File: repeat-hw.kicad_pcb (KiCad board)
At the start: 2 copper layers, 141 parts, among them J1 USB_C_Receptacle_USB2.0, J2 ARJM11C7-114-BA-EW2, J3 Conn_Coaxial, T1 FA2805, U1 nRF5340-QKxx, U10 USBLC6-2SC6, U11 USBLC6-2SC6, U2 USBLC6-2SC6, U3 W5100S, U4 TLV431DBZ, U5 VO618A, U6 SI3402, U7 nRF21540, U8 VO618A, U9 AMS1117-3.3, Y1 32MHz, Y2 25MHz

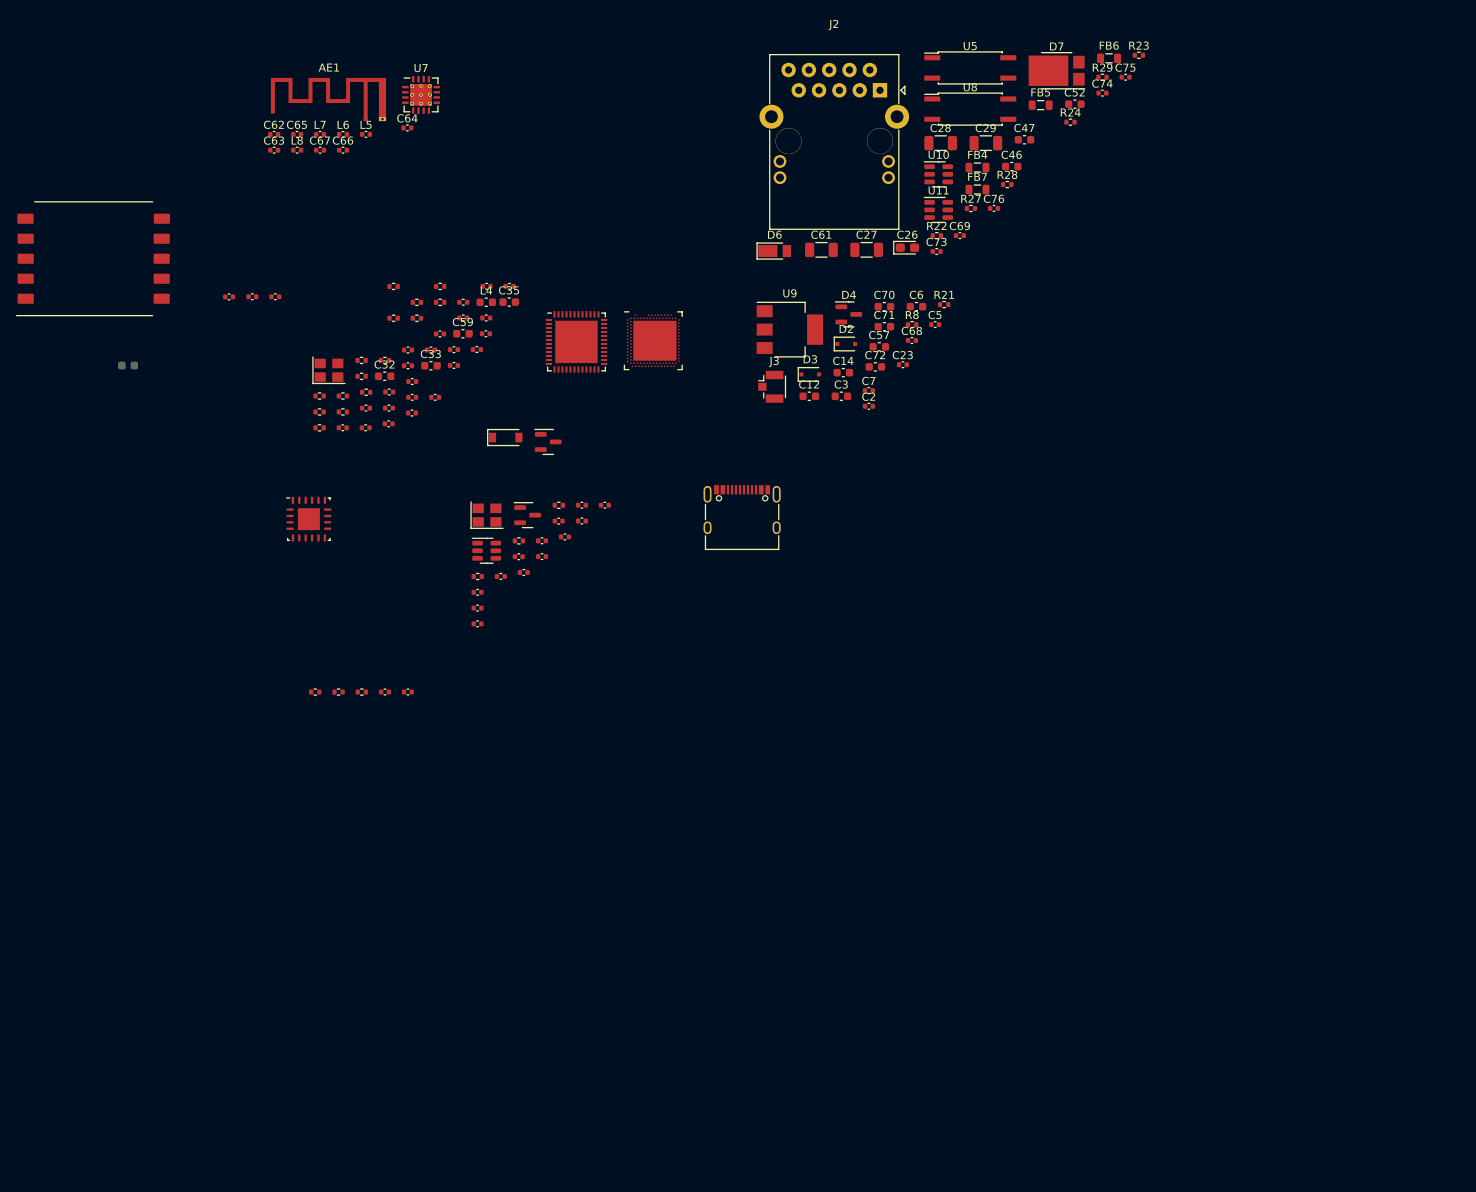
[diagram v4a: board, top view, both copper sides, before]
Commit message: Routing half done
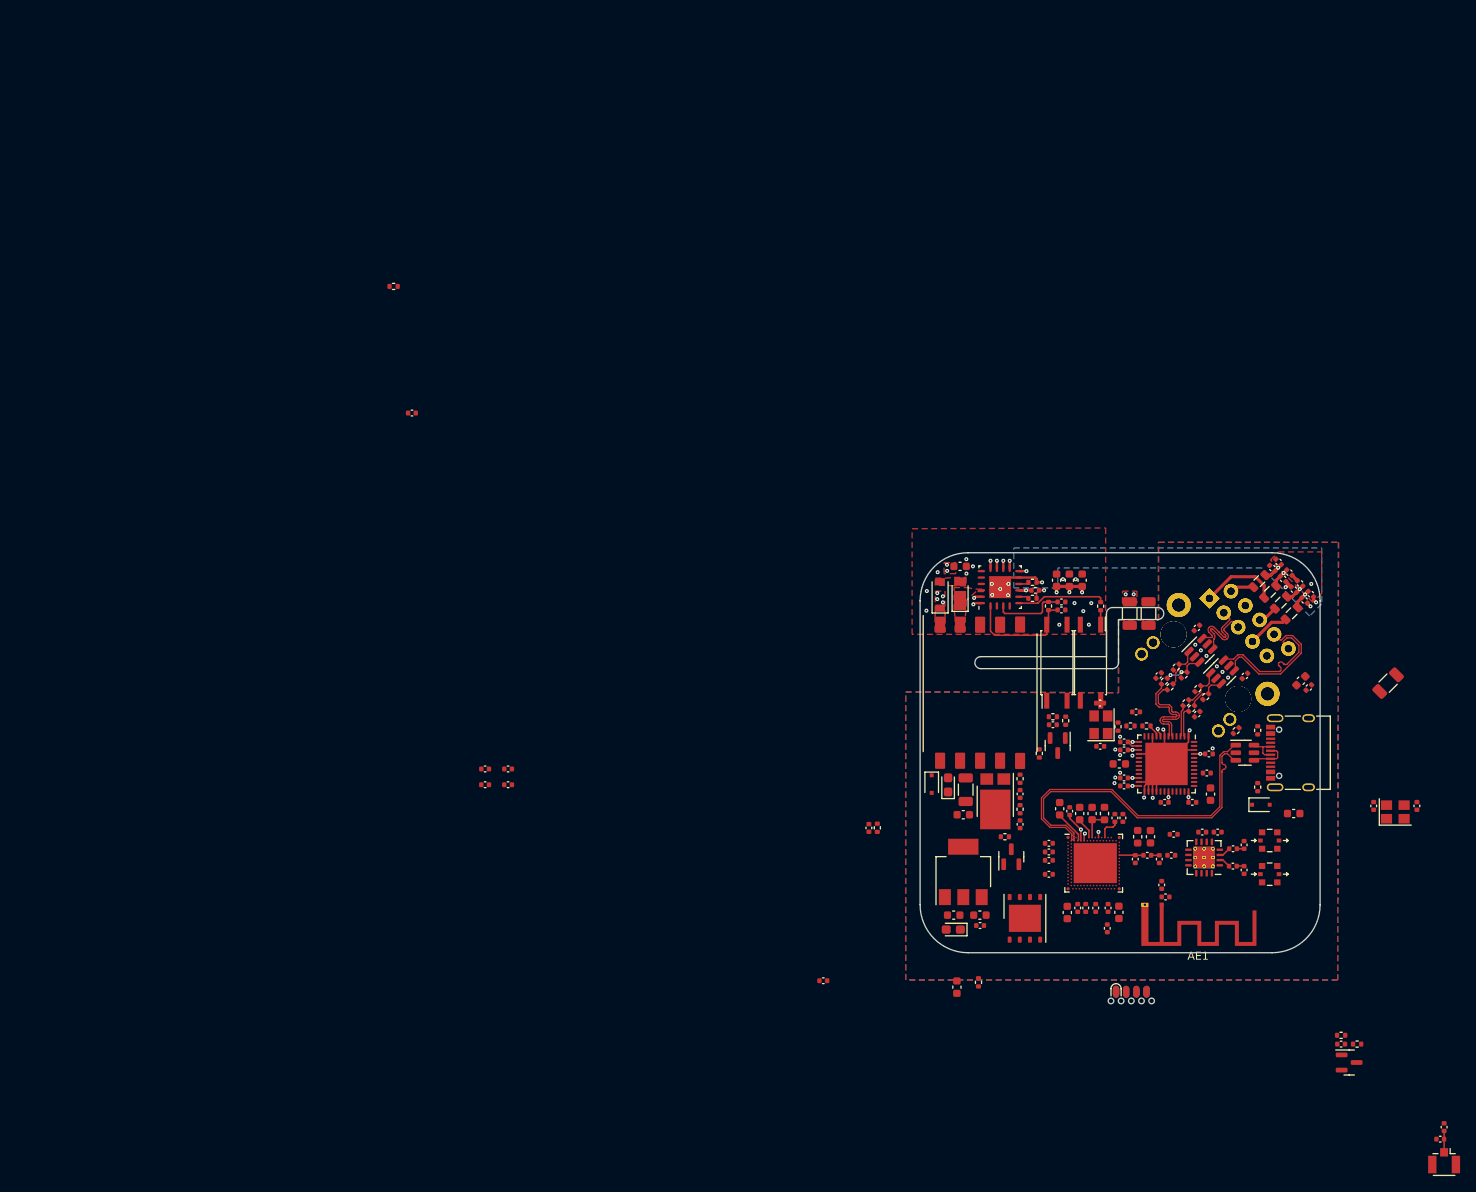
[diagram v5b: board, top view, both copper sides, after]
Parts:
- added C58: 47u, Capacitor_Tantalum_SMD:CP_EIA-2012-12_Kemet-R, F.Cu at (134.9, 126.7)
- added C77: TBD, Capacitor_SMD:C_0402_1005Metric, F.Cu at (79.3, 108.6)
- added C78: TBD, Capacitor_SMD:C_0402_1005Metric, F.Cu at (76.4, 108.6)
- added C79: TBD, Capacitor_SMD:C_0402_1005Metric, F.Cu at (79.3, 106.6)
- added C80: TBD, Capacitor_SMD:C_0402_1005Metric, F.Cu at (76.4, 106.6)
- added C81: 100n, Capacitor_SMD:C_0402_1005Metric, F.Cu at (118.7, 133.1)
- added C82: 100n, Capacitor_SMD:C_0402_1005Metric, F.Cu at (146.9, 118.0)
- added C83: 100n, Capacitor_SMD:C_0402_1005Metric, F.Cu at (156.2, 112.8)
- added C84: 100n, Capacitor_SMD:C_0402_1005Metric, F.Cu at (149.5, 111.9)
- added J2: ARJM11C7-114-BA-EW2, abracon:ARJM11C7-114-BA-EW2, B.Cu at (166.5, 93.8)
- added J4: Programming header, soicbite:SOIC_clipProgSmall, F.Cu at (157.2, 133.7)
- added L1: 10u, Inductor_SMD:L_0603_1608Metric, F.Cu at (158.0, 115.1)
- added L3: 10u, Inductor_SMD:L_0603_1608Metric, F.Cu at (153.8, 112.2)
- added TP1: MM8130-2600, murrata:MM8130-2600, F.Cu at (174.5, 115.6)
- added TP2: MM8130-2600, murrata:MM8130-2600, F.Cu at (174.5, 119.8)
- added U12: MX25R3235FZNxx0, Package_SON:WSON-8-1EP_6x5mm_P1.27mm_EP3.4x4mm, F.Cu at (143.9, 125.3)
- C1: moved to F.Cu
- C31: footprint Capacitor_SMD:C_0402_1005Metric -> Capacitor_SMD:C_0603_1608Metric
- C46, C47: value 3u3 -> 4u7
- J2: moved to B.Cu
- J3: value Conn_Coaxial -> ANT2
- moved C63 191.1 mm to (195.8, 152.9), turned to 180 degrees
- moved L6 185.3 mm to (196.3, 151.4), turned to 90 degrees
- moved C65 148.0 mm to (171.3, 116.1), turned to 90 degrees
- moved C62 146.6 mm to (161.5, 122.6)
- moved L7 146.2 mm to (169.9, 118.8), turned to 180 degrees
- moved L8 146.0 mm to (169.9, 116.6), turned to 180 degrees
- moved AE1 139.8 mm to (161.0, 123.6), turned to 180 degrees
- moved C64 139.8 mm to (171.3, 119.3), turned to -90 degrees
- moved C49 139.7 mm to (178.9, 85.6), turned to -45 degrees
- moved C67 139.4 mm to (166.1, 114.5), turned to 180 degrees
- moved C66 138.6 mm to (168.0, 114.5)
- moved L5 136.7 mm to (161.0, 121.1), turned to 90 degrees
- moved U7 136.6 mm to (166.3, 117.7), turned to 180 degrees
- moved R3 135.2 mm to (183.4, 139.9)
- moved R4 132.0 mm to (185.4, 141.0)
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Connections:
- net /~{SPIM_CS} renamed /~{ETH_CS}
- net Net-(J2-Pad3) renamed /W5100 + PoE/CON_RD-
- net Net-(J2-Pad5) renamed /W5100 + PoE/CON_RD+
- AE1 pad 1: GND -> Net-(C62-Pad1)
- AE1 pad 2: Net-(AE1-Pad2) -> GND
- C62 pad 1: Net-(AE1-Pad2) -> Net-(C62-Pad1)
- J2 pad 10: Net-(J2-Pad10) -> /W5100 + PoE/CON_TD+
- J2 pad 8: Net-(J2-Pad8) -> /W5100 + PoE/CON_TD-
- L5 pad 1: Net-(AE1-Pad2) -> Net-(C62-Pad1)
- L5 pad 2: Net-(C64-Pad1) -> Net-(L5-Pad2)
- L6 pad 2: Net-(C65-Pad1) -> Net-(L6-Pad2)
- U1 pad AK10: unconnected-(U1-PadAK10) -> /QSPI2
- U1 pad AK12: unconnected-(U1-PadAK12) -> /QSPI_CLK
- U1 pad AK14: unconnected-(U1-PadAK14) -> /~{QSPI_CS}
- U1 pad AK16: unconnected-(U1-PadAK16) -> /~{ETH_RST}
- U1 pad AK18: unconnected-(U1-PadAK18) -> /FEM_MODE
- U1 pad AK20: unconnected-(U1-PadAK20) -> /FEM_RXEN
- U1 pad AK28: unconnected-(U1-PadAK28) -> /FEM_ANTSEL
- U1 pad AK8: unconnected-(U1-PadAK8) -> /QSPI1
- U1 pad AL13: unconnected-(U1-PadAL13) -> /~{ETH_INT}
- U1 pad AL15: unconnected-(U1-PadAL15) -> /~{FEM_CS}
- U1 pad AL27: unconnected-(U1-PadAL27) -> /FEM_TXEN
- U1 pad AL29: unconnected-(U1-PadAL29) -> /~{FEM_PDN}
- U1 pad AL5: /~{INT} -> /QSPI0
- U1 pad AL9: unconnected-(U1-PadAL9) -> /QSPI3
- U1 pad V2: unconnected-(U1-PadV2) -> /USENSE_USB
- U1 pad Y2: unconnected-(U1-PadY2) -> /USENSE_POE
- U11 pad 1: /W5100 + PoE/TD- -> /W5100 + PoE/TD+
- U11 pad 3: /W5100 + PoE/TD+ -> /W5100 + PoE/TD-
- U11 pad 4: Net-(J2-Pad10) -> /W5100 + PoE/CON_TD-
- U11 pad 6: Net-(J2-Pad8) -> /W5100 + PoE/CON_TD+
- U3 pad 2: /W5100 + PoE/TD- -> /W5100 + PoE/ESD_TD-
- U3 pad 3: /W5100 + PoE/TD+ -> /W5100 + PoE/ESD_TD+
- U3 pad 47: /~{INT} -> /~{ETH_INT}
- U3 pad 48: /~{RESET} -> /~{ETH_RST}
- U3 pad 49: (no net) -> GND
- U3 pad 5: /W5100 + PoE/RD- -> /W5100 + PoE/ESD_RD-
- U3 pad 6: /W5100 + PoE/RD+ -> /W5100 + PoE/ESD_RD+
- U6 pad 21: (no net) -> Net-(C45-Pad2)
- U7 pad 11: unconnected-(U7-Pad11) -> /~{FEM_PDN}
- U7 pad 12: unconnected-(U7-Pad12) -> /SPIM_CLK
- U7 pad 13: unconnected-(U7-Pad13) -> /SPIM_MOSI
- U7 pad 14: unconnected-(U7-Pad14) -> /SPIM_MISO
- U7 pad 15: unconnected-(U7-Pad15) -> /~{FEM_CS}
- U7 pad 4: unconnected-(U7-Pad4) -> /FEM_MODE
- U7 pad 7: unconnected-(U7-Pad7) -> /FEM_RXEN
- U7 pad 8: unconnected-(U7-Pad8) -> /FEM_ANTSEL
- U7 pad 9: unconnected-(U7-Pad9) -> /FEM_TXEN
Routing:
- net Net-(C50-Pad2): track 0.00 -> 44.8 mm, vias 0 -> 2
- net Net-(C54-Pad2): track 0.00 -> 43.8 mm, vias 0 -> 2
- net Net-(C48-Pad2): track 0.00 -> 43.5 mm, vias 0 -> 2
- net /ESD_D-: track 0.00 -> 41.6 mm
- net /ESD_D+: track 0.00 -> 41.6 mm
- net GND: track 0.00 -> 40.5 mm, vias 0 -> 18
- net Net-(C44-Pad2): track 0.00 -> 35.2 mm, vias 0 -> 2
- net /W5100 + PoE/CON_TD+: track 0.00 -> 17.2 mm
- net /W5100 + PoE/CON_TD-: track 0.00 -> 17.1 mm
- net Net-(C34-Pad1): track 0.00 -> 14.7 mm
- net /W5100 + PoE/ESD_RD+: track 0.00 -> 11.6 mm
- net /W5100 + PoE/ESD_RD-: track 0.00 -> 11.4 mm
- net Net-(R28-Pad2): track 0.00 -> 11.1 mm
- net Net-(C28-Pad2): track 0.00 -> 11.0 mm, vias 0 -> 16
- net Net-(FB4-Pad2): track 0.00 -> 9.96 mm
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- added copper zone on B.Cu, net GND
- added copper zone on F.Cu, net GND
- added copper zone on In1.Cu, net GND
- added copper zone on In4.Cu, net GND
- added copper zone on F.Cu, net Net-(C28-Pad2)
- added copper zone on In2.Cu, net Net-(C28-Pad2)
- added copper zone on F.Cu, net Net-(C29-Pad2)
- added copper zone on F.Cu, net Net-(C32-Pad2)
- added copper zone on In1.Cu, net Net-(C32-Pad2)
- added copper zone on In4.Cu, net Net-(C32-Pad2)
- added copper zone on B.Cu, net Net-(C45-Pad2)
- added copper zone on F.Cu, net Net-(D5-Pad2)
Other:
- board outline added: 50 x 50 mm
- copper layers 2 -> 6

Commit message: More routing
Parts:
- moved C7 11.0 mm to (133.9, 116.2)
- moved C58 9.67 mm to (137.2, 117.3), turned to 0 degrees
- moved C70 9.56 mm to (137.2, 115.6), turned to 0 degrees
- moved C57 8.64 mm to (133.9, 117.5)
- moved D2 3.69 mm to (132.5, 112.2), turned to 90 degrees
- moved U9 3.26 mm to (136.0, 122.8), turned to -90 degrees
- moved C26 1.80 mm to (132.5, 108.6)
- moved L4 0.76 mm to (135.8, 113.0), turned to 90 degrees
- moved C27 0.70 mm to (135.8, 109.2)
- moved D7 0.64 mm to (139.6, 110.7)
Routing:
- net /W5100 + PoE/5V: track 0.00 -> 1.07 mm, vias 0 -> 3
- net GND: vias 18 -> 37
- net +3V3: vias 4 -> 15
- added copper zone on F.Cu, net +3V3
- added copper zone on F.Cu, net +5V
- added copper zone on F.Cu, net /W5100 + PoE/5V
- added copper zone on In2.Cu, net /W5100 + PoE/5V
- added copper zone on F.Cu, net Net-(C27-Pad1)
- added copper zone on F.Cu, net Net-(D7-Pad1)

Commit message: Routing almost done
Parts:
- AE1: footprint RF_Antenna:Texas_SWRA117D_2.4GHz_Left -> RF_Antenna:Texas_SWRA117D_2.4GHz_Right
- C26: value 470u -> 220u; footprint Capacitor_Tantalum_SMD:CP_EIA-2012-12_Kemet-R -> Capacitor_SMD:CP_Elec_5x5.3
- C58: value 47u -> 10u; footprint Capacitor_Tantalum_SMD:CP_EIA-2012-12_Kemet-R -> Capacitor_SMD:C_0603_1608Metric
- moved R25 107.4 mm to (162.1, 92.2)
- moved C56 98.8 mm to (159.0, 98.8), turned to 180 degrees
- moved C77 66.4 mm to (127.8, 154.0)
- moved C78 66.4 mm to (124.9, 154.0)
- moved C79 66.4 mm to (127.8, 152.0)
- moved C80 66.4 mm to (124.9, 152.0)
- moved J3 46.9 mm to (159.2, 127.0)
- moved L6 46.9 mm to (159.2, 122.8)
- moved C63 46.9 mm to (158.7, 124.2)
- moved C4 38.7 mm to (154.3, 108.2)
- moved C9 38.7 mm to (148.9, 108.2)
- moved Y1 38.7 mm to (151.6, 108.9)
- moved C10 35.2 mm to (159.2, 119.3), turned to 0 degrees
- moved R2 32.8 mm to (157.7, 119.8), turned to 90 degrees
- moved C23 30.9 mm to (178.3, 110.5)
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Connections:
- C29 pad 2: Net-(C29-Pad2) -> Earth
- C45 pad 2: Net-(C45-Pad2) -> Earth
- C49 pad 2: Net-(C45-Pad2) -> Earth
- C51 pad 2: Net-(C45-Pad2) -> Earth
- C55 pad 2: Net-(C45-Pad2) -> Earth
- D6 pad 1: Net-(C29-Pad2) -> Net-(D6-Pad1)
- L5 pad 2: Net-(L5-Pad2) -> Net-(TP2-PadA)
- L6 pad 2: Net-(L6-Pad2) -> Net-(TP1-PadA)
- R16 pad 2: Net-(C45-Pad2) -> Earth
- T1 pad 2: Net-(C29-Pad2) -> Net-(D6-Pad1)
- TP1 pad A: Net-(L5-Pad2) -> Net-(TP1-PadA)
- TP2 pad A: Net-(L6-Pad2) -> Net-(TP2-PadA)
- U6 pad 18: Net-(C29-Pad2) -> Net-(D6-Pad1)
- U6 pad 21: Net-(C45-Pad2) -> Earth
- U6 pad 9: Net-(C45-Pad2) -> Earth
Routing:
- net +3V3: track 7.22 -> 51.7 mm, vias 15 -> 31
- net /SPIM_MISO: track 0.00 -> 40.6 mm, vias 0 -> 4
- net /SPIM_MOSI: track 0.00 -> 35.6 mm, vias 0 -> 3
- net /SPIM_CLK: track 0.00 -> 32.8 mm, vias 0 -> 3
- net /FEM_MODE: track 0.00 -> 32.2 mm, vias 0 -> 2
- net /~{FEM_CS}: track 0.00 -> 27.1 mm, vias 0 -> 1
- net +3V3A: track 2.45 -> 26.5 mm, vias 2 -> 15
- net /FEM_RXEN: track 0.00 -> 20.4 mm, vias 0 -> 2
- net /~{ETH_CS}: track 0.00 -> 19.8 mm, vias 0 -> 2
- net /W5100 + PoE/ACT: track 0.00 -> 18.5 mm, vias 0 -> 1
- net /FEM_TXEN: track 0.00 -> 17.9 mm, vias 0 -> 2
- net /QSPI3: track 0.00 -> 17.4 mm
- net /USENSE_POE: track 0.00 -> 16.4 mm, vias 0 -> 2
- net /FEM_ANTSEL: track 0.00 -> 16.4 mm, vias 0 -> 2
- net VBUS: track 0.00 -> 15.9 mm, vias 0 -> 8
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- added copper zone on In3.Cu, net +1V2
- added copper zone on In2.Cu, net +3V3
- added copper zone on In2.Cu, net +3V3A
- added copper zone on B.Cu, net Earth
- added copper zone on F.Cu, net Earth
- added copper zone on In1.Cu, net Earth
- added copper zone on In4.Cu, net Earth
- added copper zone on B.Cu, net Net-(C31-Pad2)
- added copper zone on In3.Cu, net Net-(C31-Pad2)
- added copper zone on F.Cu, net Net-(D6-Pad1)
- added copper zone on In2.Cu, net VBUS
- removed copper zone on F.Cu, net Net-(C29-Pad2)
- removed copper zone on In1.Cu, net Net-(C31-Pad2)
- removed copper zone on In4.Cu, net Net-(C31-Pad2)
- removed copper zone on B.Cu, net Net-(C45-Pad2)

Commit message: Routing done
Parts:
- added TP3: TestPoint, TestPoint:TestPoint_Pad_D1.0mm, F.Cu at (141.2, 115.8)
- added TP4: TestPoint, TestPoint:TestPoint_Pad_D1.0mm, F.Cu at (139.0, 115.8)
- moved C77 38.9 mm to (143.0, 118.2), turned to -90 degrees
- moved C78 37.9 mm to (142.0, 120.1), turned to -90 degrees
- moved C80 36.7 mm to (143.0, 120.1), turned to -90 degrees
- moved C79 36.7 mm to (142.0, 118.2), turned to -90 degrees
- moved C46 17.0 mm to (156.8, 99.6), turned to 90 degrees
- moved J4 2.30 mm to (151.6, 129.2), turned to 0 degrees
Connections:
- U1 pad B24: unconnected-(U1-PadB24) -> /PLOSS
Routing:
- net +5V: track 3.94 -> 60.0 mm, vias 0 -> 7
- net /~{ETH_RST}: track 1.01 -> 53.7 mm
- net VBUS: track 15.9 -> 63.6 mm, vias 8 -> 9
- net /~{ETH_INT}: track 5.53 -> 52.2 mm, vias 1 -> 2
- net /USENSE_USB: track 3.67 -> 40.8 mm, vias 1 -> 2
- net /PLOSS: track 0.00 -> 19.3 mm, vias 0 -> 2
- net /SWDIO: track 0.00 -> 17.6 mm, vias 0 -> 2
- net /SWDCLK: track 0.00 -> 14.6 mm, vias 0 -> 2
- net /NFC2: track 0.00 -> 13.4 mm
- net /~{RESET}: track 3.24 -> 16.5 mm, vias 0 -> 2
- net /NFC1: track 0.00 -> 10.9 mm
- net Net-(L3-Pad2): track 2.03 -> 8.20 mm
- net +3V3: track 51.7 -> 53.5 mm, vias 31 -> 32
- net +1V2: track 8.09 -> 9.69 mm, vias 4 -> 6
- net /QSPI3: track 17.4 -> 16.3 mm
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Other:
- board text added: "REPEAT V1.0 20.11.2022"
- board text added: "Vojtěch Vosáhlo"
